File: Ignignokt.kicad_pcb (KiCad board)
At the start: 2 copper layers, 324 x 356 mm, 277 parts, among them J1 Barrel_Jack_Switch, J2 Conn_01x02_Pin, Q1 IRLB8721PBF, Q2 FQP27P06, U1 LM2585S-12, U2 LM2937ET-5.0, U3 PIC12F675-IMC

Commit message: Small tweaks to board
The MOSFET for the LEDs was a TO-247 which did not match the part I had selected. Changed it to a TO-220 to match the part. Also added a pull-down resistor to the gate to ensure it turns off when there is no longer a voltage on the pin. The PIC chip will ground it but it makes sense to have the extra part in case the board is used without it.

Signed-off-by: Nathan Hjelm <hjelmn@me.com>
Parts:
- added R68: 100k, Resistor_THT:R_Axial_DIN0207_L6.3mm_D2.5mm_P10.16mm_Horizontal, F.Cu at (67.0, 297.0)
- Q1: footprint Package_TO_SOT_THT:TO-247-3_Vertical -> Package_TO_SOT_THT:TO-220-3_Vertical
- R1, R10, R11, R12, R13, R14, R15, R16, R17, R18, R19, R2, R20, R21, R22, R23, R24, R25, R26, R27, R28, R3, R30, R31, R32, R33, R34, R35, R36, R37, R38, R39, R4, R40, R41, R42, R43, R44, R45, R46, R47, R48, R49, R5, R50, R51, R52, R53, R54, R55, R57, R58, R59, R6, R60, R61, R62, R63, R7, R8, R9: value 76 -> 120
- R29: value 180 -> 300
- R65: value 200 -> 400
- moved Q1 11.7 mm to (67.0, 304.2), turned to 180 degrees
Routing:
- net Net-(Q1-G): track 32.5 -> 22.1 mm
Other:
- board text added: "v0.1"
- board text removed: "v0"

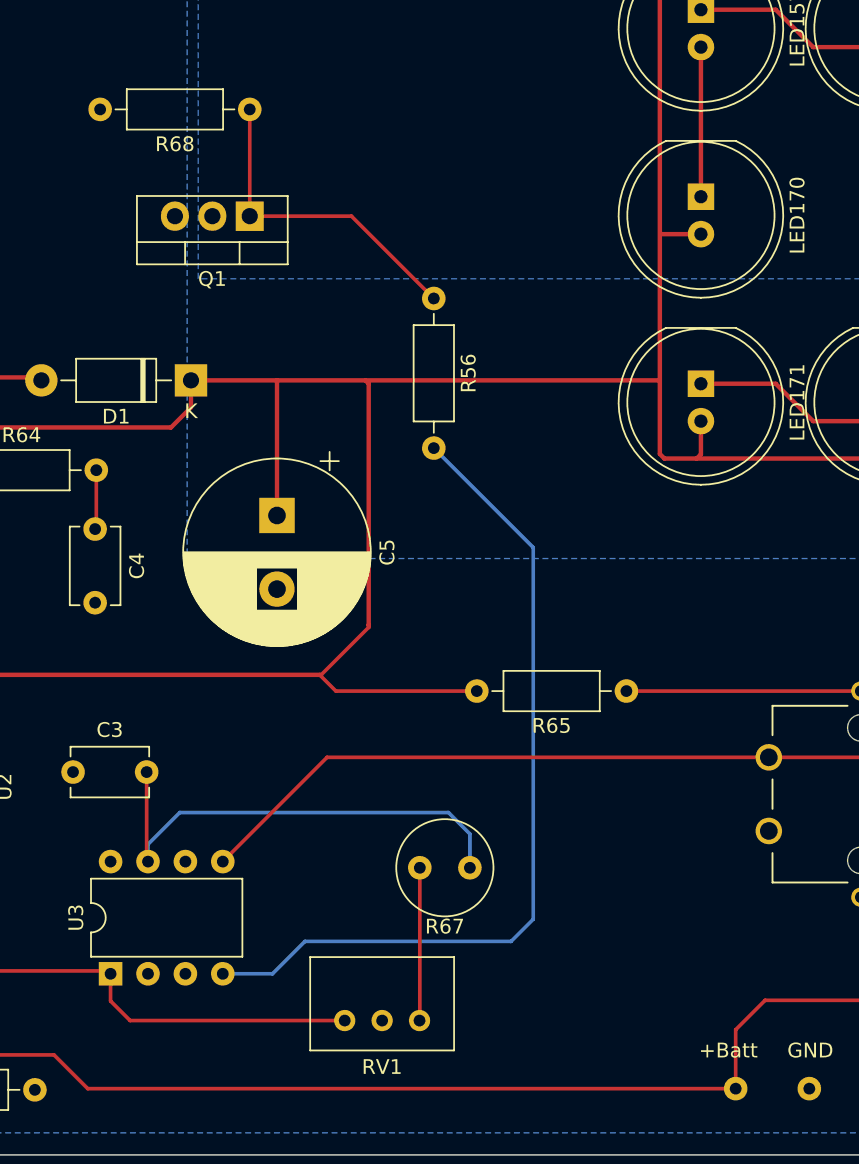
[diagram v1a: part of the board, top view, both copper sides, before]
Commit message: Small tweaks
The original schematic I used to design the board erroneously used pin 4 (GPIO3) as an output pin. This will not work with a PIC2F675 as that pin is input-only. Moved the output to GPIO4 to correct the issue and adjusted some other components based on observations.

To fix the boards I have I put a jumper between GPIO3 and GPIO4 and disabled external MCLR to avoid the output causing a reset of the chip.

Also, can use a 200 ohm resistor in place of the potentiometer (dropped to 1k). 10k might be a bit too high but could work as well. Will do more calculations to see what is best since the 10k can only go down to 5.3k. At 200 ohm it takes about 8 clock cycles for the GPIO pin to register high at the appropriate light level.

Signed-off-by: Nathan Hjelm <hjelmn@me.com>
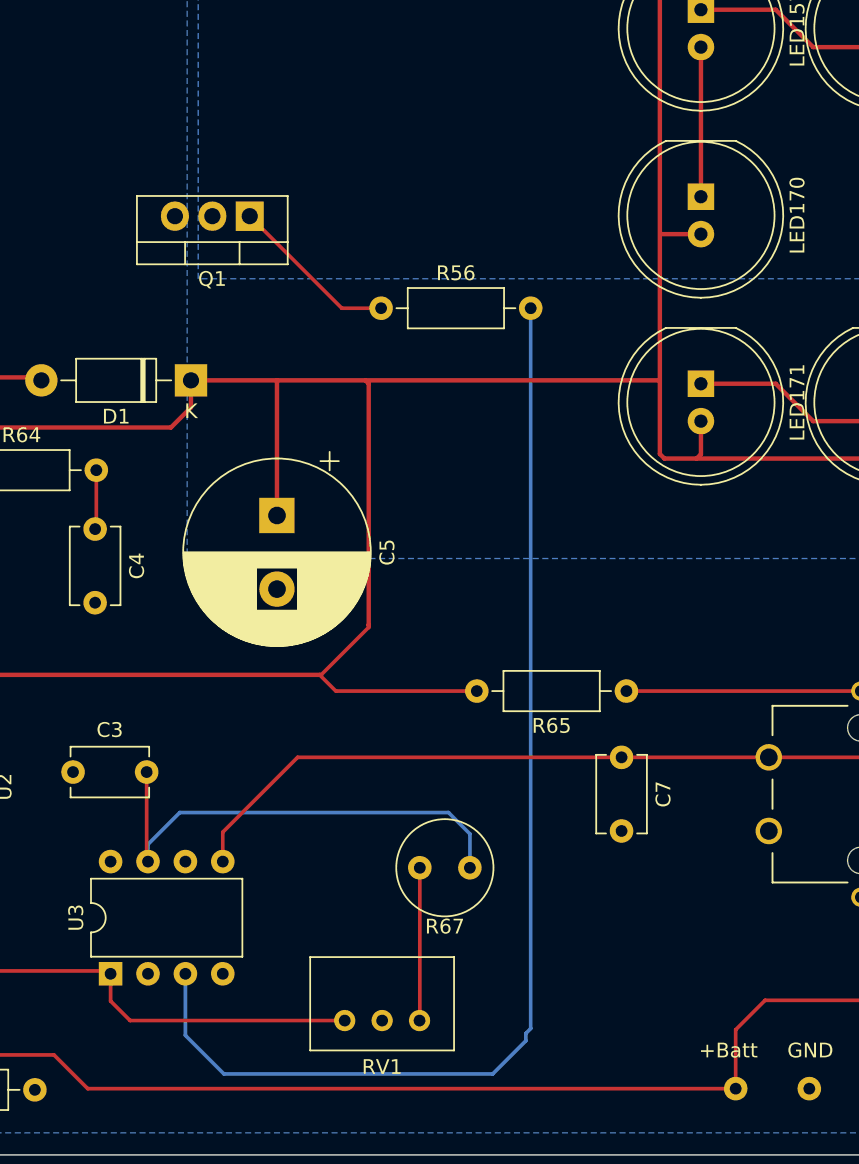
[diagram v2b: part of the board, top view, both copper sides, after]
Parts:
- removed R68: 100k, Resistor_THT:R_Axial_DIN0207_L6.3mm_D2.5mm_P10.16mm_Horizontal
- added C7: 1µF, Capacitor_THT:C_Disc_D5.1mm_W3.2mm_P5.00mm, F.Cu at (92.2, 341.0)
- moved R56 3.64 mm to (75.9, 310.5), turned to 0 degrees
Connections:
- R56 pad 2: Net-(U3-GP3) -> Net-(U3-GP4)
- U3 pad 3: unconnected-(U3-GP4-Pad3) -> Net-(U3-GP4)
- U3 pad 4: Net-(U3-GP3) -> unconnected-(U3-GP3-Pad4)
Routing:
- net Net-(U3-GP4): track 0.00 -> 79.2 mm
- net Net-(U3-GP3): track 57.4 -> 0.00 mm
- net Net-(Q1-G): track 22.1 -> 11.5 mm
- net Net-(U3-GP2): track 52.5 -> 53.7 mm

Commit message: Update with a 4:0 LEDs:resistors ratio
After closer inspection it seems the original sign was using a 4:1 ratio given there are 3 resistors for each eye/eyebrow (12 LEDS), 3 for the right arm (12 LEDs), etc. The LEDs I ordered also appear to be 2.6-2.9v forward voltage drop (not the 3-3.2 advetised) so it is better to do 4 LEDs to one 64 ohm resistor to get ~ 10mA of current. These LEDs are super bright so running close to 20mA would be a mistake.

Signed-off-by: Nathan Hjelm <hjelmn@me.com>
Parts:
- removed the R11 at (48.9, 87.0)
- removed the R14 at (116.5, 90.4)
- removed the R17 at (215.8, 90.1)
- removed the R18 at (252.5, 112.5)
- removed the R22 at (326.2, 117.2)
- removed the R29 at (59.5, 167.0)
- removed the R3 at (122.8, 34.4)
- removed the R35 at (41.8, 201.9)
- removed the R37 at (127.2, 208.9)
- removed the R4 at (212.3, 23.5)
- removed the R46 at (181.5, 217.0)
- removed the R48 at (135.7, 256.6)
- removed the R51 at (265.0, 256.4)
- removed R55, R59: 120, Resistor_THT:R_Axial_DIN0207_L6.3mm_D2.5mm_P10.16mm_Horizontal
- added RV1: 1k, Potentiometer_THT:Potentiometer_Bourns_3299W_Vertical, F.Cu at (82.9, 325.4)
- C5: footprint Capacitor_THT:CP_Radial_D12.5mm_P5.00mm -> Capacitor_THT:CP_Radial_D18.0mm_P7.50mm
- R1, R2: value 120 -> 76
- R10: renamed from R13; value 120 -> 76
- R11: renamed from R15; value 120 -> 76
- R12: renamed from R16; value 120 -> 76
- R13: renamed from R23; value 120 -> 76
- R14: renamed from R30; value 120 -> 76
- R15: renamed from R19; value 120 -> 76
- R16: renamed from R20; value 120 -> 76
- R17: renamed from R31; value 120 -> 76
- R18: renamed from R24; value 120 -> 76
- R19: renamed from R27; value 120 -> 76
- R20: renamed from R21; value 120 -> 340
- R21: renamed from R25; value 120 -> 76
- R22: renamed from R26; value 120 -> 76
- R23: renamed from R28; value 120 -> 76
- R24: renamed from R36; value 120 -> 76
- R25: renamed from R32; value 120 -> 76
- R26: renamed from R34; value 120 -> 76
- R27: renamed from R33; value 120 -> 76
- R28: renamed from R45; value 120 -> 76
- R29: renamed from R38; value 120 -> 76
- R3: renamed from R10; value 120 -> 76
- R30: renamed from R39; value 120 -> 76
- R31: renamed from R42; value 120 -> 76
- R32: renamed from R44; value 120 -> 76
- R33: renamed from R43; value 120 -> 76
- R34: renamed from R40; value 120 -> 76
- R35: renamed from R41; value 120 -> 76
- R36: renamed from R47; value 120 -> 76
- R37: renamed from R49; value 120 -> 76
- R38: renamed from R50; value 120 -> 76
- R39: renamed from R52; value 120 -> 76
- R4: renamed from R5; value 120 -> 76
- R40: renamed from R53; value 120 -> 340
- R41: renamed from R60; value 120 -> 76
- R42: renamed from R54; value 120 -> 76
- R43: renamed from R62; value 120 -> 340
- R45: renamed from R57; value 120 -> 76
- R46: renamed from R58; value 120 -> 76
- R47: renamed from R63; value 120 -> 76
- R48: renamed from R61; value 120 -> 76
- R5: renamed from R6; value 120 -> 76
- R50: renamed from R65; value 400 -> 200
- R6: renamed from R7; value 120 -> 76
- R7: renamed from R8; value 120 -> 76
- R8: renamed from R9; value 120 -> 76
- R9: renamed from R12; value 120 -> 76
- RV2: renamed from RV1; value 10k -> 1k
- moved R33 134.5 mm to (159.0, 217.5), turned to 180 degrees
- moved R8 42.1 mm to (186.5, 40.0), turned to 0 degrees
- moved R17 39.6 mm to (196.7, 135.5), turned to 0 degrees
- moved R1 37.2 mm to (135.8, 16.0), turned to 180 degrees
- moved R14 32.8 mm to (136.1, 135.5)
- moved R30 29.0 mm to (210.5, 211.0)
- moved R19 27.5 mm to (290.0, 117.0), turned to 90 degrees
- moved R2 27.1 mm to (158.8, 19.2)
- moved R35 25.2 mm to (265.5, 226.8), turned to -90 degrees
- moved R41 24.5 mm to (145.8, 277.5), turned to -90 degrees
- moved R43 24.2 mm to (196.5, 277.8), turned to -90 degrees
- moved R4 23.5 mm to (224.8, 16.0)
- moved R48 23.0 mm to (224.8, 306.5), turned to 180 degrees
- moved R16 20.8 mm to (206.0, 118.7), turned to -90 degrees
- moved R42 20.2 mm to (202.2, 277.8), turned to -90 degrees
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- renumbered C7 to C6, C6 to C7, LED102 to LED100, LED103 to LED102, LED100 to LED103, LED107 to LED106, LED106 to LED107, LED110 to LED109, LED13 to LED11, LED109 to LED110, LED118 to LED117, LED117 to LED118, LED120 to LED119, LED11 to LED12, LED119 to LED120, LED122 to LED121, LED121 to LED122, LED124 to LED123, LED123 to LED124, LED126 to LED125, LED125 to LED126, LED128 to LED127, LED127 to LED128, LED12 to LED13, LED132 to LED131, LED131 to LED132, LED137 to LED136, LED136 to LED137, LED143 to LED142, LED142 to LED143, LED147 to LED146, LED146 to LED147, LED149 to LED148, LED148 to LED149, LED16 to LED15, LED160 to LED158, LED15 to LED16, LED158 to LED160, LED164 to LED163, LED163 to LED164, LED19 to LED17, LED172 to LED170, LED170 to LED172, LED177 to LED176, LED176 to LED177, LED179 to LED178, LED178 to LED179, LED183 to LED182, LED182 to LED183, LED185 to LED184, LED184 to LED185, LED17 to LED19, LED21 to LED20, LED20 to LED21, LED23 to LED22, LED22 to LED23, LED26 to LED25, LED25 to LED26, LED29 to LED28, LED28 to LED29, LED37 to LED36, LED36 to LED37, LED39 to LED38, LED38 to LED39, LED43 to LED42, LED42 to LED43, LED47 to LED46, LED46 to LED47, LED50 to LED48, LED48 to LED50, LED54 to LED53, LED55 to LED54, LED53 to LED55, LED57 to LED56, LED56 to LED57, LED61 to LED59, LED7 to LED6, LED59 to LED60, LED62 to LED61, LED60 to LED62, LED65 to LED64, LED64 to LED65, LED69 to LED68, LED68 to LED69, LED6 to LED7, LED75 to LED72, LED72 to LED73, LED73 to LED75, LED79 to LED78, LED78 to LED79, LED9 to LED8, LED82 to LED81, LED81 to LED82, LED84 to LED83, LED83 to LED84, LED86 to LED85, LED85 to LED86, LED89 to LED87, LED87 to LED89, LED8 to LED9, LED95 to LED93, LED93 to LED94, LED94 to LED95, LED99 to LED96, LED96 to LED97, LED97 to LED98, LED98 to LED99, R56 to R44, R64 to R49, R66 to R51, R67 to R52
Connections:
- LED100 pad 1: Net-(LED102-K) -> Net-(LED100-K)
- LED100 pad 2: +12V -> Net-(LED100-A)
- LED101 pad 1: Net-(LED101-K) -> Net-(LED100-A)
- LED102 pad 1: Net-(LED103-K) -> Net-(LED102-K)
- LED102 pad 2: Net-(LED102-K) -> Net-(LED102-A)
- LED103 pad 1: Net-(LED100-K) -> Net-(LED102-A)
- LED107 pad 2: +12V -> Net-(LED105-A)
- LED109 pad 1: Net-(LED110-K) -> Net-(LED109-K)
- LED109 pad 2: +12V -> Net-(LED109-A)
- LED11 pad 2: +12V -> Net-(LED105-A)
- LED110 pad 1: Net-(LED109-K) -> Net-(LED109-A)
- LED111 pad 2: Net-(LED110-K) -> Net-(LED105-A)
- LED114 pad 2: +12V -> Net-(LED112-K)
- LED116 pad 2: Net-(LED113-K) -> Net-(LED115-K)
- LED117 pad 2: +12V -> Net-(LED117-A)
- LED118 pad 1: Net-(LED117-K) (its old number) -> Net-(LED117-A)
- LED118 pad 2: Net-(LED117-A) -> Net-(LED105-A)
- LED119 pad 2: +12V -> Net-(LED105-A)
- LED121 pad 2: +12V -> Net-(LED105-A)
- LED123 pad 1: Net-(LED105-A) -> Net-(LED123-K)
- LED123 pad 2: +12V -> Net-(LED123-A)
- LED124 pad 1: Net-(LED123-K) -> Net-(LED123-A)
- LED125 pad 2: +12V -> Net-(LED125-A)
- LED127 pad 1: Net-(LED127-A) (its old number) -> Net-(LED127-K)
- LED128 pad 1: Net-(LED127-K) -> Net-(LED125-A)
- LED128 pad 2: Net-(LED127-A) (its old number) -> Net-(LED105-A)
- LED130 pad 2: +12V -> Net-(LED129-K)
- LED131 pad 1: Net-(LED131-A) -> Net-(LED131-K)
- LED131 pad 2: +12V -> Net-(LED105-A)
- LED132 pad 2: Net-(LED131-A) -> Net-(LED105-A)
- LED133 pad 2: +12V -> Net-(LED131-K)
- LED134 pad 2: +12V -> Net-(LED134-A)
- LED135 pad 1: Net-(LED117-A) -> Net-(LED135-K)
- LED136 pad 2: +12V -> Net-(LED105-A)
- LED139 pad 2: +12V -> Net-(LED105-A)
- LED140 pad 2: +12V -> Net-(LED140-A)
- LED141 pad 1: Net-(LED141-K) -> Net-(LED140-A)
- LED142 pad 1: Net-(LED143-K) -> Net-(LED142-K)
- LED143 pad 2: Net-(LED140-K) -> Net-(LED105-A)
- LED144 pad 2: +12V -> Net-(LED142-K)
- LED146 pad 1: Net-(LED147-K) (its old number) -> Net-(LED146-K)
- LED146 pad 2: Net-(LED145-K) -> Net-(LED105-A)
- LED147 pad 2: +12V -> Net-(LED146-K)
- LED151 pad 2: +12V -> Net-(LED105-A)
- LED153 pad 2: +12V -> Net-(LED152-K)
- LED154 pad 2: Net-(LED153-K) -> Net-(LED105-A)
- LED155 pad 1: Net-(LED155-K) -> Net-(LED134-A)
- LED156 pad 2: Net-(LED156-A) -> Net-(LED105-A)
- LED157 pad 1: Net-(LED156-A) -> Net-(LED157-K)
- LED157 pad 2: Net-(LED157-A) -> Net-(LED105-A)
- LED160 pad 2: +12V -> Net-(LED156-K)
- LED167 pad 2: +12V -> Net-(LED167-A)
- LED168 pad 1: Net-(LED168-K) -> Net-(LED167-A)
- LED168 pad 2: Net-(LED168-A) -> Net-(LED105-A)
- LED169 pad 1: Net-(LED168-A) -> Net-(LED169-K)
- LED169 pad 2: Net-(LED169-A) -> Net-(LED105-A)
- LED170 pad 1: Net-(LED172-K) -> Net-(LED170-K)
- LED171 pad 2: +12V -> Net-(LED171-A)
- LED172 pad 1: Net-(LED157-A) -> Net-(LED171-A)
- LED172 pad 2: +12V -> Net-(LED157-K)
- LED173 pad 2: Net-(LED172-K) -> Net-(LED173-A)
- LED174 pad 1: Net-(LED174-K) -> Net-(LED173-A)
- LED174 pad 2: +12V -> Net-(LED174-A)
- LED175 pad 2: +12V -> Net-(LED105-A)
- LED176 pad 1: Net-(LED177-K) -> Net-(LED176-K)
- LED176 pad 2: Net-(LED176-K) -> Net-(LED105-A)
- LED177 pad 1: Net-(LED176-K) -> Net-(LED174-A)
- LED177 pad 2: Net-(LED174-K) -> Net-(LED176-K)
- LED178 pad 2: +12V -> Net-(LED105-A)
- LED179 pad 2: +12V -> Net-(LED105-A)
- LED18 pad 2: +12V -> Net-(LED18-A)
- LED182 pad 1: Net-(LED183-K) -> Net-(LED182-K)
- LED182 pad 2: Net-(LED182-K) -> Net-(LED182-A)
- LED183 pad 1: Net-(LED182-K) -> Net-(LED183-K)
- LED183 pad 2: +12V -> Net-(LED181-K)
- LED184 pad 1: Net-(LED185-K) -> Net-(LED182-A)
- LED184 pad 2: Net-(LED183-K) -> Net-(LED184-A)
- LED185 pad 1: Net-(LED169-A) -> Net-(LED184-A)
- LED185 pad 2: +12V -> Net-(LED169-K)
- LED19 pad 1: Net-(LED17-K) -> Net-(LED18-A)
- LED19 pad 2: +12V -> Net-(LED105-A)
- LED2 pad 2: Net-(LED17-K) -> Net-(LED105-A)
- LED20 pad 2: +12V -> Net-(LED105-A)
- LED21 pad 1: Net-(LED20-K) (its old number) -> GND1
- LED21 pad 2: Net-(LED20-A) -> Net-(LED105-A)
- LED22 pad 1: Net-(LED20-A) -> Net-(LED22-K)
- LED22 pad 2: Net-(LED23-A) -> GND1
- LED23 pad 1: Net-(LED22-K) -> Net-(LED23-K)
- LED23 pad 2: +12V -> Net-(LED23-A)
- LED24 pad 2: +12V -> Net-(LED22-K)
- LED25 pad 2: Net-(LED22-K) -> Net-(LED105-A)
- LED26 pad 1: Net-(LED25-K) (its old number) -> Net-(LED26-K)
- LED27 pad 2: +12V -> Net-(LED26-K)
- LED29 pad 2: +12V -> Net-(LED29-A)
- LED30 pad 2: Net-(LED30-A) -> Net-(LED105-A)
- LED31 pad 2: +12V -> Net-(LED30-K)
- LED32 pad 1: Net-(LED32-K) -> Net-(LED29-A)
- LED32 pad 2: Net-(LED32-A) -> Net-(LED105-A)
- LED33 pad 1: Net-(LED32-A) -> Net-(LED33-K)
- LED35 pad 1: Net-(LED30-A) -> Net-(LED35-K)
- LED36 pad 1: Net-(LED37-K) -> Net-(LED36-K)
- LED37 pad 2: +12V -> Net-(LED36-K)
- LED38 pad 1: Net-(LED39-K) -> Net-(LED38-K)
- LED38 pad 2: Net-(LED39-A) (its old number) -> Net-(LED38-A)
- LED39 pad 1: Net-(LED38-K) -> Net-(LED38-A)
- LED4 pad 1: Net-(LED4-K) -> Net-(LED3-A)
- LED4 pad 2: Net-(LED3-K) -> Net-(LED1-K)
- LED41 pad 2: Net-(LED41-A) -> Net-(LED40-K)
- LED42 pad 2: +12V -> Net-(LED42-A)
- LED43 pad 1: Net-(LED42-K) -> Net-(LED42-A)
- LED45 pad 2: +12V -> Net-(LED105-A)
- LED46 pad 2: Net-(LED46-K) -> Net-(LED105-A)
- LED47 pad 1: Net-(LED46-K) -> Net-(LED47-K)
- LED47 pad 2: +12V -> Net-(LED47-A)
- LED48 pad 2: +12V -> Net-(LED105-A)
- LED50 pad 2: +12V -> Net-(LED50-A)
- LED51 pad 1: Net-(LED39-A) (its old number) -> Net-(LED51-K)
- LED52 pad 1: Net-(LED41-A) -> Net-(LED52-K)
- LED53 pad 2: +12V -> Net-(LED53-A)
- LED54 pad 2: +12V -> Net-(LED105-A)
- LED56 pad 2: Net-(LED56-K) -> Net-(LED105-A)
- LED57 pad 1: Net-(LED56-K) -> Net-(LED57-K)
- LED57 pad 2: +12V -> Net-(LED57-A)
- LED59 pad 1: Net-(LED61-K) -> Net-(LED59-K)
- LED59 pad 2: Net-(LED59-K) -> Net-(LED59-A)
- LED6 pad 1: Net-(LED3-A) -> Net-(LED6-K)
- LED6 pad 2: +12V -> Net-(LED6-A)
- LED60 pad 1: Net-(LED59-K) -> Net-(LED60-K)
- LED60 pad 2: +12V -> Net-(LED60-A)
- LED61 pad 1: Net-(LED60-A) -> Net-(LED61-K)
- LED61 pad 2: +12V -> Net-(LED60-K)
- LED62 pad 2: Net-(LED60-A) -> Net-(LED59-K)
- LED63 pad 1: Net-(LED63-K) -> Net-(LED59-A)
- LED63 pad 2: Net-(LED61-K) -> Net-(LED105-A)
- LED65 pad 1: Net-(LED64-K) (its old number) -> Net-(LED47-A)
- LED66 pad 1: Net-(LED66-K) -> Net-(LED50-A)
- LED66 pad 2: +12V -> Net-(LED66-A)
- LED67 pad 2: +12V -> Net-(LED105-A)
- LED68 pad 1: Net-(LED69-K) -> Net-(LED66-A)
- LED68 pad 2: Net-(LED66-K) -> Net-(LED105-A)
- LED69 pad 1: Net-(LED68-K) -> Net-(LED69-K)
- LED7 pad 1: Net-(LED6-K) -> Net-(LED6-A)
- LED72 pad 1: Net-(LED72-A) -> Net-(LED72-K)
- LED72 pad 2: +12V -> Net-(LED72-A)
- LED73 pad 2: Net-(LED72-A) -> Net-(LED105-A)
- LED74 pad 1: Net-(LED73-A) -> Net-(LED72-A)
- LED74 pad 2: +12V -> Net-(LED74-A)
- LED75 pad 1: Net-(LED73-K) (its old number) -> Net-(LED74-A)
- LED75 pad 2: Net-(LED73-A) -> Net-(LED75-A)
- LED76 pad 1: Net-(LED76-K) -> Net-(LED53-A)
- LED77 pad 1: Net-(LED77-K) -> Net-(LED75-A)
- LED77 pad 2: Net-(LED73-K) (its old number) -> Net-(LED105-A)
- LED79 pad 1: Net-(LED78-K) (its old number) -> Net-(LED57-A)
- LED8 pad 1: Net-(LED8-A) -> Net-(LED8-K)
- LED80 pad 2: +12V -> Net-(LED105-A)
- LED81 pad 2: +12V -> Net-(LED105-A)
- LED82 pad 1: Net-(LED81-K) (its old number) -> Net-(LED82-K)
- LED83 pad 1: Net-(LED84-K) -> Net-(LED83-K)
- LED83 pad 2: Net-(LED83-K) -> Net-(LED82-K)
- LED84 pad 1: Net-(LED83-K) -> Net-(LED60-A)
- LED85 pad 1: Net-(LED86-K) (its old number) -> Net-(LED85-K)
- LED85 pad 2: Net-(LED103-K) -> Net-(LED105-A)
- LED87 pad 1: Net-(LED89-K) -> Net-(LED87-K)
- LED89 pad 2: +12V -> Net-(LED104-K)
- LED9 pad 1: Net-(LED8-K) -> Net-(LED9-K)
- LED9 pad 2: Net-(LED8-A) -> Net-(LED10-K)
- LED90 pad 2: +12V -> Net-(LED85-K)
- LED91 pad 2: +12V -> Net-(LED105-A)
- LED92 pad 2: +12V -> Net-(LED105-A)
- LED93 pad 1: Net-(LED95-K) (its old number) -> Net-(LED93-K)
- LED93 pad 2: Net-(LED115-K) -> Net-(LED93-A)
- LED97 pad 2: +12V -> Net-(LED105-A)
- LED99 pad 1: Net-(LED98-K) -> Net-(LED93-A)
- R1 pad 1: Net-(LED1-K) -> Net-(LED3-K)
- R10 pad 1: Net-(LED37-K) -> Net-(LED35-K)
- R12 pad 1: Net-(LED40-K) -> Net-(LED41-K)
- R13 pad 1: Net-(LED64-K) (its old number) -> Net-(LED47-K)
- R14 pad 1: Net-(LED68-K) -> Net-(LED71-K)
- R15 pad 1: Net-(LED71-K) -> Net-(LED51-K)
- R16 pad 1: Net-(LED76-K) -> Net-(LED52-K)
- R17 pad 1: Net-(LED77-K) -> Net-(LED72-K)
- R18 pad 1: Net-(LED78-K) (its old number) -> Net-(LED57-K)
- R21 pad 1: Net-(LED81-K) (its old number) -> Net-(LED83-K)
- R22 pad 1: Net-(LED84-K) -> Net-(LED61-K)
- R24 pad 1: Net-(LED104-K) -> Net-(LED87-K)
- R26 pad 1: Net-(LED100-K) -> Net-(LED102-K)
- R27 pad 1: Net-(LED101-K) -> Net-(LED100-K)
- R28 pad 1: Net-(LED127-K) -> Net-(LED108-K)
- R3 pad 1: Net-(LED25-K) (its old number) -> Net-(LED8-K)
- R30 pad 1: Net-(LED112-K) -> Net-(LED113-K)
- R31 pad 1: Net-(LED98-K) -> Net-(LED93-K)
- R33 pad 1: Net-(LED95-K) (its old number) -> Net-(LED127-K)
- R35 pad 1: Net-(LED117-K) (its old number) -> Net-(LED135-K)
- R36 pad 1: Net-(LED141-K) -> Net-(LED140-K)
- R37 pad 1: Net-(LED147-K) (its old number) -> Net-(LED145-K)
- R39 pad 1: Net-(LED152-K) -> Net-(LED153-K)
- R4 pad 1: Net-(LED10-K) -> Net-(LED9-K)
- R46 pad 1: Net-(LED156-K) -> Net-(LED170-K)
- R47 pad 1: Net-(LED185-K) -> Net-(LED182-K)
- R48 pad 1: Net-(LED181-K) -> Net-(LED183-K)
- R50 pad 2: +12V -> +5V
- R8 pad 1: Net-(LED20-K) (its old number) -> Net-(LED23-K)
- R9 pad 1: Net-(LED32-K) -> Net-(LED33-K)
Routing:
- net +12V: track 2279.0 -> 109.4 mm
- net Net-(LED105-A): track 10.2 -> 2105.2 mm
- net Net-(LED115-K): track 85.0 -> 10.2 mm
- net +5V: track 58.4 -> 106.1 mm
- net Net-(LED81-K) (its old number): track 32.4 -> 0.00 mm
- net Net-(LED84-K): track 31.5 -> 0.00 mm
- net Net-(LED163-K): track 38.0 -> 10.1 mm
- net Net-(LED159-K): track 37.2 -> 10.0 mm
- net Net-(LED39-K): track 25.7 -> 0.00 mm
- net Net-(LED101-K): track 25.3 -> 0.00 mm
- net Net-(LED170-K): track 0.00 -> 24.4 mm
- net Net-(LED18-A): track 0.00 -> 24.3 mm
- net Net-(LED185-K): track 22.7 -> 0.00 mm
- net Net-(LED93-K): track 0.00 -> 21.5 mm
- net Net-(LED100-K): track 7.49 -> 28.6 mm
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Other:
- board text added: "v0.2"
- board text removed: "v0.1"

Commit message: Small tweaks
Signed-off-by: Nathan Hjelm <hjelmn@me.com>
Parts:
- Q1, Q2: footprint Package_TO_SOT_THT:TO-220-3_Vertical -> Package_TO_SOT_THT:TO-220-3_Horizontal_TabDown
- moved Q2 15.9 mm to (50.5, 362.5)
- moved Q1 15.5 mm to (67.0, 288.8)
- moved R51 11.5 mm to (53.6, 365.2)
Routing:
- net Net-(Q1-G): track 11.5 -> 29.2 mm
- net Net-(D2-K): track 125.3 -> 140.9 mm
- net +BATT: track 91.2 -> 75.9 mm
- net VCC: track 18.0 -> 32.6 mm

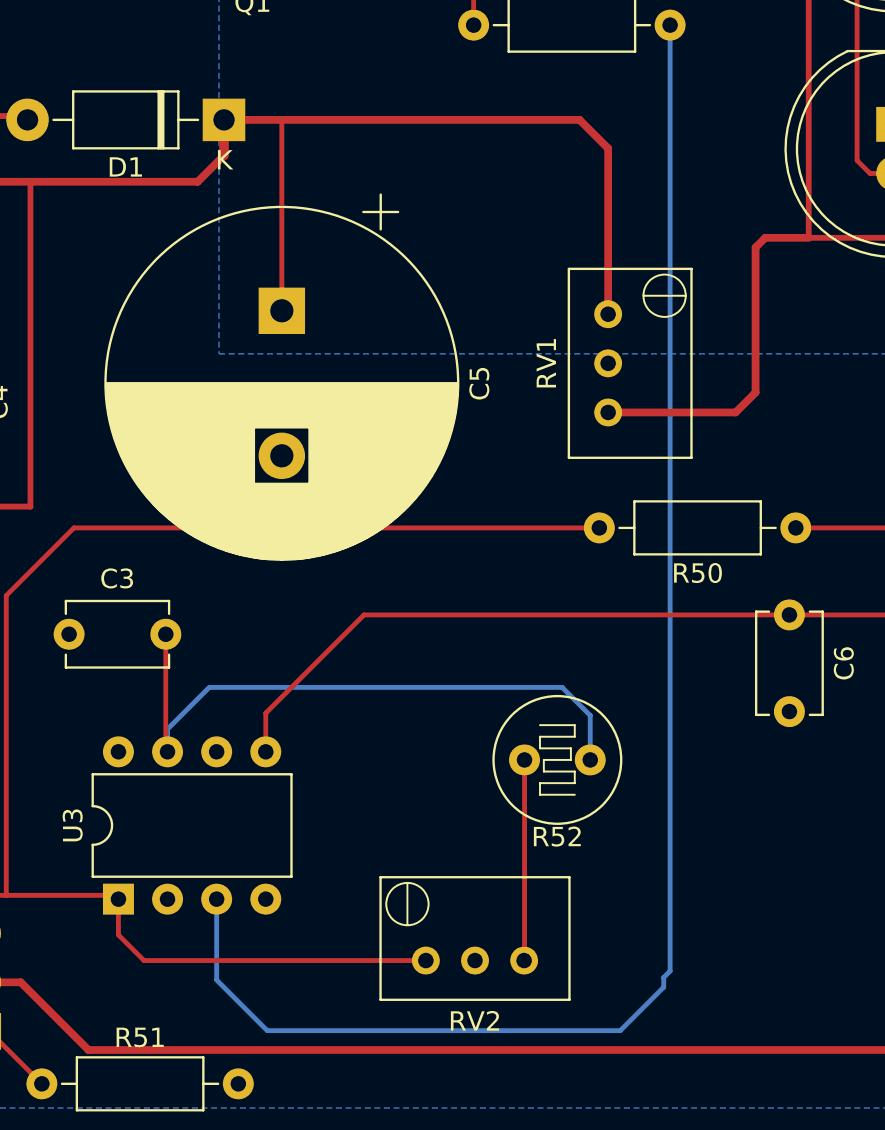
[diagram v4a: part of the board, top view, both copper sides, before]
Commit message: Fix potentiometer issues
Screwed up the schematic for the potentiometers. The middle lead should be connected to power not the right lead. No lead should be connected to ground.

Signed-off-by: Nathan Hjelm <hjelmn@me.com>
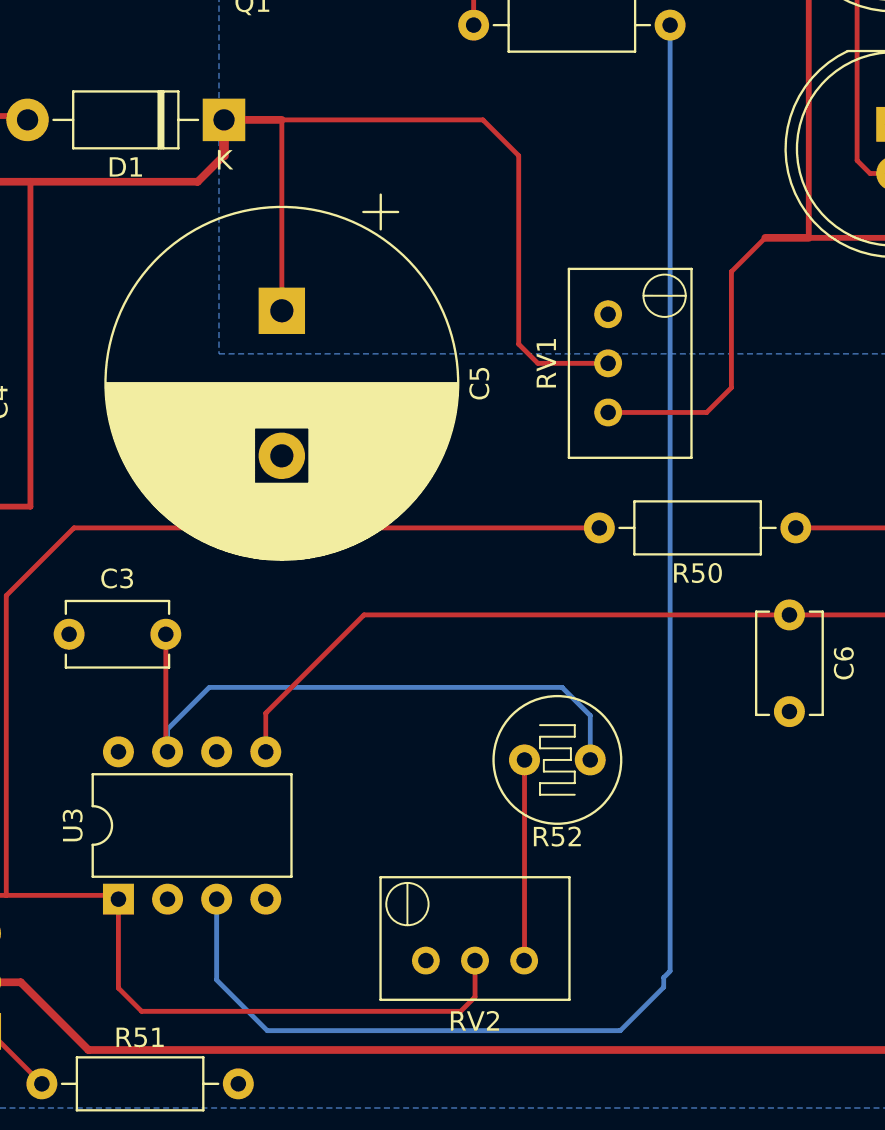
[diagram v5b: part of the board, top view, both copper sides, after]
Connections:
- LED21 pad 1: GND1 -> Net-(LED21-K)
- LED22 pad 2: GND1 -> Net-(LED21-K)
- RV1 pad 1: +12V -> unconnected-(RV1-Pad1)
- RV1 pad 2: GND -> +12V
- RV2 pad 1: +5V -> unconnected-(RV2-Pad1)
- RV2 pad 2: GND -> +5V
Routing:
- net Net-(LED21-K): track 0.00 -> 13.8 mm
- net GND1: track 13.8 -> 0.00 mm
- net +5V: track 106.1 -> 113.5 mm
- net +12V: track 109.4 -> 111.1 mm
- net Net-(LED105-A): track 2105.2 -> 2104.3 mm
